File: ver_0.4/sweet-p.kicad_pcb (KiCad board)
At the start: 2 copper layers, 80 x 75 mm, 39 parts, among them J10 Micro_SD_Card, J2 Screw_Terminal_01x02, J3 Conn_01x04_Female, J4 Conn_01x04_Female, J5 Screw_Terminal_01x05, J7 Conn_01x06_Pin, U1 adafruit_tpl511x, U4 ssd1306, U7 ds3231, U8 P78A05-1000

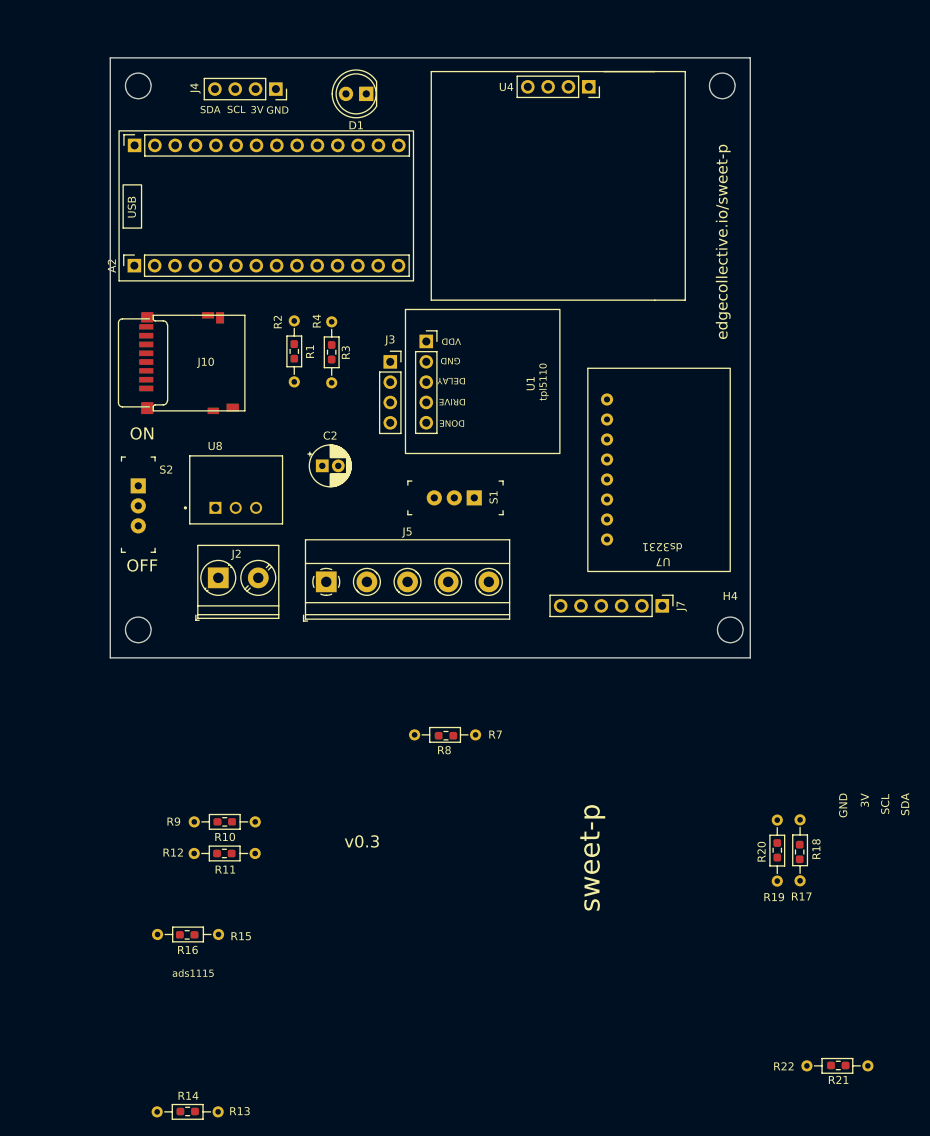
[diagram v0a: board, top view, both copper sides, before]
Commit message: pin assignments and initial layout for ver 0.4
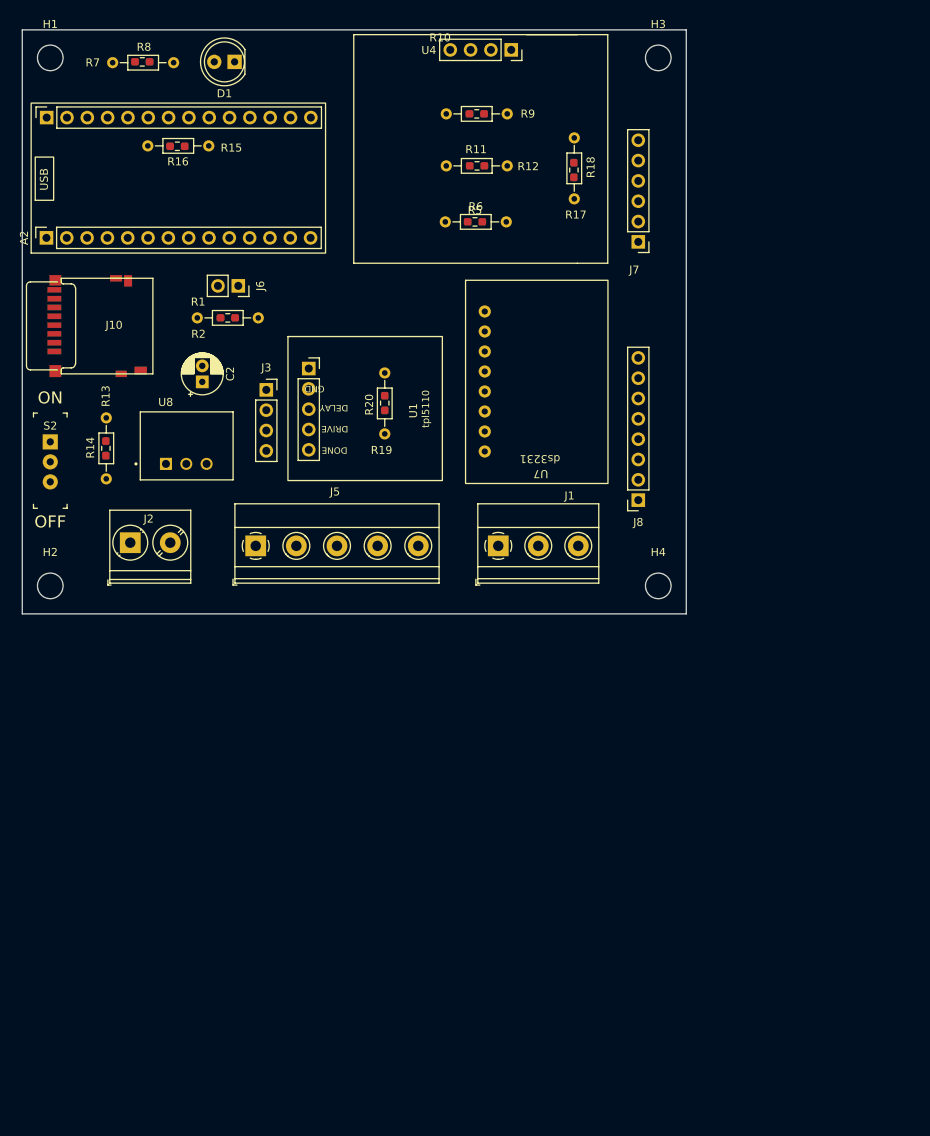
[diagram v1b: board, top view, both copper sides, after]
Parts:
- removed J4: Conn_01x04_Female, Connector_PinSocket_2.54mm:PinSocket_1x04_P2.54mm_Vertical
- removed R21: 10K, Resistor_SMD:R_0603_1608Metric_Pad0.98x0.95mm_HandSolder
- removed R22: R, Resistor_THT:R_Axial_DIN0204_L3.6mm_D1.6mm_P7.62mm_Horizontal
- removed R3: 4.7K, Resistor_SMD:R_0603_1608Metric_Pad0.98x0.95mm_HandSolder
- removed R4: 4.7K, Resistor_THT:R_Axial_DIN0204_L3.6mm_D1.6mm_P7.62mm_Horizontal
- removed S1: EG1218, digikey-footprints:Switch_Slide_11.6x4mm_EG1218
- added J1: Screw_Terminal_01x03, TerminalBlock_Phoenix:TerminalBlock_Phoenix_MKDS-1,5-3_1x03_P5.00mm_Horizontal, F.Cu at (85.0, 86.0)
- added J6: Conn_01x02_Socket, Connector_PinSocket_2.54mm:PinSocket_1x02_P2.54mm_Vertical, F.Cu at (52.5, 53.5)
- added J8: Conn_01x08_Socket, Connector_PinSocket_2.54mm:PinSocket_1x08_P2.54mm_Vertical, F.Cu at (102.5, 80.3)
- added R5: 4.7K, Resistor_SMD:R_0603_1608Metric_Pad0.98x0.95mm_HandSolder, F.Cu at (82.1, 45.5)
- added R6: 4.7K, Resistor_THT:R_Axial_DIN0204_L3.6mm_D1.6mm_P7.62mm_Horizontal, F.Cu at (78.4, 45.5)
- C2: value C_Polarized -> 330uF
- moved H2 104.7 mm to (29.0, 91.0)
- moved R16 98.6 mm to (44.9, 36.0)
- moved R15 98.6 mm to (41.2, 36.0)
- moved H3 96.6 mm to (105.0, 25.0)
- moved R7 95.5 mm to (36.8, 25.6), turned to 0 degrees
- moved R10 93.9 mm to (82.3, 32.0), turned to 0 degrees
- moved R8 92.4 mm to (40.5, 25.5), turned to 0 degrees
- moved R9 91.7 mm to (78.5, 32.0), turned to 0 degrees
- moved R11 91.6 mm to (82.3, 38.5), turned to 0 degrees
- moved R17 89.8 mm to (94.5, 42.6)
- moved R18 89.8 mm to (94.5, 39.0)
- moved R12 89.2 mm to (78.5, 38.5), turned to 0 degrees
- moved R14 83.5 mm to (36.0, 73.8), turned to 90 degrees
- moved R13 79.4 mm to (36.0, 77.6), turned to 90 degrees
- moved R19 74.4 mm to (70.8, 72.0)
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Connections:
- A2 pad 10: unconnected-(A2-A5-Pad10) -> A5
- A2 pad 11: unconnected-(A2-SCK-Pad11) -> SCK
- A2 pad 12: unconnected-(A2-M0-Pad12) -> MOSI
- A2 pad 13: unconnected-(A2-MI-Pad13) -> MISO
- A2 pad 14: unconnected-(A2-D2-Pad14) -> RX_D2
- A2 pad 20: unconnected-(A2-7-Pad20) -> DONE
- A2 pad 21: unconnected-(A2-9-Pad21) -> SAT_EN
- A2 pad 23: RX2 -> ONEWIRE_11
- A2 pad 24: TX2 -> D12
- A2 pad 4: unconnected-(A2-VHI-Pad4) -> VHI
- A2 pad 6: SAT_EN -> BATT_A1
- A2 pad 7: A1 -> A2
- A2 pad 8: DONE -> A3
- A2 pad 9: A4 -> TX_A4
- J10 pad 9: unconnected-(J10-SHIELD-Pad9) -> GND
- J5 pad 3: RX -> RX_D2
- J5 pad 4: TX -> TX_A4
- J5 pad 5: A4 -> D12
- J7 pad 4: TX2 -> TX
- J7 pad 5: RX2 -> RX
- R1 pad 1: Net-(R1-Pad1) -> Net-(J3-Pin_2)
- R13 pad 2: A1 -> BATT_A1
- R14 pad 2: A1 -> BATT_A1
- R15 pad 1: A1 -> BATT_A1
- R16 pad 1: A1 -> BATT_A1
- R2 pad 1: Net-(R1-Pad1) -> Net-(J3-Pin_2)
- U7 pad 7: RTC_INT -> unconnected-(U7-SQW-Pad7)
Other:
- board size 80 x 75 mm -> 83 x 73 mm
- board text removed: "3V"
- board text removed: "SCL"
- board text removed: "SDA"
- board text removed: "VDD"
- board text removed: "ads1115"
- board text removed: "edgecollective.io/sweet-p"
- board text removed: "sweet-p"
- board text removed: "v0.3"

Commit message: fully routed v4
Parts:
- moved J6 3.46 mm to (49.0, 53.5)
- moved R1 3.46 mm to (47.7, 57.5)
- moved R2 3.46 mm to (51.5, 57.5)
- moved R15 3.08 mm to (40.5, 39.0)
- moved R16 3.08 mm to (44.2, 39.0)
- moved U8 2.06 mm to (41.4, 75.5)
- moved C2 1.07 mm to (47.8, 64.5)
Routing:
- net GND: track 0.00 -> 320.9 mm, vias 0 -> 11
- net +3V3: track 0.00 -> 229.7 mm, vias 0 -> 13
- net SDA: track 0.00 -> 124.3 mm, vias 0 -> 8
- net 5V_TIMER: track 0.00 -> 112.9 mm, vias 0 -> 6
- net ONEWIRE_11: track 0.00 -> 107.1 mm, vias 0 -> 3
- net SCL: track 0.00 -> 105.0 mm, vias 0 -> 4
- net D12: track 0.00 -> 104.6 mm, vias 0 -> 2
- net 5V_DC: track 0.00 -> 90.7 mm, vias 0 -> 3
- net A0: track 0.00 -> 87.6 mm, vias 0 -> 1
- net A2: track 0.00 -> 87.4 mm, vias 0 -> 3
- net A3: track 0.00 -> 81.7 mm, vias 0 -> 3
- net SAT_EN: track 0.00 -> 71.3 mm, vias 0 -> 2
- net DONE: track 0.00 -> 68.4 mm, vias 0 -> 4
- net A5: track 0.00 -> 67.0 mm, vias 0 -> 2
- net TX_A4: track 0.00 -> 63.4 mm, vias 0 -> 2
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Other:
- board text added: "1W"
- board text added: "3V"
- board text added: "5V"
- board text added: "A0"
- board text added: "A2"
- board text added: "A3"
- board text added: "A5"
- board text added: "D12"
- board text added: "DRX"
- board text added: "DTX"
- board text added: "RX"
- board text added: "SCL"
- board text added: "SDA"
- board text added: "SEN"
- board text added: "TX"
- board text added: "VEXT"
- board text added: "itsybitsy"
- board text added: "p78a05-1000"
- board text added: "ssd1306"

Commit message: update
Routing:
- net D12: track 104.6 -> 99.6 mm, vias 2 -> 0
- net SCL: track 105.0 -> 107.2 mm
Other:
- board text added: "RX2"
- board text added: "TX2"
- board text added: "github.com/edgecollective/sweet-p"
- board text added: "sweet-p ver 0.4"
- board text removed: "DRX"
- board text removed: "DTX"
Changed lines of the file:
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@@
 	)
 	(gr_rect
+		(start 56 52.75)
+		(end 76.5 55.75)
+		(stroke
+			(width 0.15)
+			(type default)
+		)
+		(fill none)
+		(layer "F.SilkS")
+	)
+	(gr_rect
 		(start 25.5 21.5)
 		(end 108.5 94.5)
@@
 		(layer "Edge.Cuts")
 	)
+	(gr_text "github.com/edgecollective/sweet-p"
+		(at 105.6 79.9 -90)
+		(layer "B.SilkS")
+		(effects
+			(font
+				(size 1.5 1.5)
+				(thickness 0.3)
+				(bold yes)
+			)
+			(justify left bottom mirror)
+		)
+	)
 	(gr_text "1W"
 		(at 88.75 93.25 0)
@@
 		)
 	)
+	(gr_text "sweet-p ver 0.4"
+		(at 56.75 55 0)
+		(layer "F.SilkS")
+		(effects
+			(font
+				(size 1.5 1.5)
+				(thickness 0.3)
+				(bold yes)
+			)
+			(justify left bottom)
+		)
+	)
 	(gr_text "3V"
 		(at 104.75 48.5 0)
@@
 		)
 	)
-	(gr_text "DRX"
+	(gr_text "RX2"
 		(at 63.5 93.5 0)
 		(layer "F.SilkS")
@@
 		)
 	)
-	(gr_text "DTX"
+	(gr_text "TX2"
 		(at 68.5 93.5 0)
 		(layer "F.SilkS")
@@
 	)
 	(segment
-		(start 83.2575 38.5)
-		(end 86.12 38.5)
+		(start 89.002 71.162)
+		(end 90.5 72.66)
 		(width 0.4)
 		(layer "F.Cu")
@@
 	)
 	(segment
-		(start 55 36)
-		(end 83.62 36)
+		(start 83.2575 38.5)
+		(end 86.12 38.5)
 		(width 0.4)
 		(layer "F.Cu")
@@
 	)
 	(segment
-		(start 89.16 72.66)
-		(end 88.5 72)
+		(start 89 71.162)
+		(end 89.002 71.162)
 		(width 0.4)
 		(layer "F.Cu")
@@
 	)
 	(segment
-		(start 87 61.5)
-		(end 86.8 61.7)
+		(start 88.3 61.7)
+		(end 88.9 61.1)
 		(width 0.4)
 		(layer "F.Cu")
@@
 	)
 	(segment
-		(start 87.5 61.5)
-		(end 87 61.5)
+		(start 55 36)
+		(end 83.62 36)
 		(width 0.4)
 		(layer "F.Cu")
@@
 	)
 	(segment
-		(start 86.8 61.7)
-		(end 83.31 61.7)
+		(start 83.31 61.7)
+		(end 88.3 61.7)
 		(width 0.4)
 		(layer "F.Cu")
@@
 	(segment
 		(start 102.5 72.66)
-		(end 89.16 72.66)
+		(end 90.5 72.66)
 		(width 0.4)
 		(layer "F.Cu")
@@
 	)
 	(via
-		(at 87.5 61.5)
+		(at 89 71.162)
 		(size 0.8)
 		(drill 0.4)
@@
 	)
 	(via
-		(at 88.5 72)
+		(at 88.9 61.1)
 		(size 0.8)
 		(drill 0.4)
@@
 	)
 	(segment
-		(start 88.5 62.5)
-		(end 87.5 61.5)
+		(start 88.5 44.4)
+		(end 87.9 45)
+		(width 0.4)
+		(layer "B.Cu")
+		(net 9)
+	)
+	(segment
+		(start 87.9 46.1)
+		(end 88.9 47.1)
 		(width 0.4)
 		(layer "B.Cu")
@@
 	)
 	(segment
+		(start 88.9 69.562)
+		(end 88.9 71.062)
+		(width 0.4)
+		(layer "B.Cu")
+		(net 9)
+	)
+	(segment
 		(start 86.62 39)
 		(end 86.12 38.5)
@@
 	)
 	(segment
-		(start 87.5 61.5)
-		(end 87.5 39)
+		(start 88.9 61.1)
+		(end 88.9 70)
+		(width 0.4)
+		(layer "B.Cu")
+		(net 9)
+	)
+	(segment
+		(start 88.9 70)
+		(end 88.9 69.562)
+		(width 0.4)
+		(layer "B.Cu")
+		(net 9)
+	)
+	(segment
+		(start 88.5 40)
+		(end 88.5 40.4)
+		(width 0.4)
+		(layer "B.Cu")
+		(net 9)
+	)
+	(segment
+		(start 87.9 45)
+		(end 87.9 46.1)
+		(width 0.4)
+		(layer "B.Cu")
+		(net 9)
+	)
+	(segment
+		(start 87.5 39)
+		(end 88.5 40)
 		(width 0.4)
 		(layer "B.Cu")
@@
 	)
 	(segment
+		(start 88.9 71.062)
+		(end 89 71.162)
+		(width 0.4)
+		(layer "B.Cu")
+		(net 9)
+	)
+	(segment
 		(start 53.95 32.465)
 		(end 53.95 34.95)
@@
 	)
 	(segment
-		(start 88.5 72)
-		(end 88.5 62.5)
+		(start 88.9 47.1)
+		(end 88.9 61.1)
+		(width 0.4)
+		(layer "B.Cu")
+		(net 9)
+	)
+	(segment
+		(start 88.5 40.4)
+		(end 88.5 44.4)
 		(width 0.4)
 		(layer "B.Cu")
@@
 	)
 	(segment
-		(start 74 91)
-		(end 35.5 91)
-		(width 0.4)
-		(layer "F.Cu")
-		(net 26)
-	)
-	(segment
-		(start 35.5 91)
-		(end 34.5 90)
-		(width 0.4)
-		(layer "F.Cu")
-		(net 26)
-	)
-	(via
-		(at 74 91)
-		(size 0.8)
-		(drill 0.4)
-		(layers "F.Cu" "B.Cu")
-		(net 26)
-	)
-	(via
-		(at 34.5 90)
-		(size 0.8)
-		(drill 0.4)
-		(layers "F.Cu" "B.Cu")
-		(net 26)
-	)
-	(segment
-		(start 75 86)
-		(end 75 90)
+		(start 37.39 59.61)
+		(end 34.25 62.75)
 		(width 0.4)
 		(layer "B.Cu")
@@
 	)
 	(segment
-		(start 34.8 62.2)
-		(end 37.39 59.61)
+		(start 34.25 62.75)
+		(end 34.25 87.75)
 		(width 0.4)
 		(layer "B.Cu")
@@
 	)
 	(segment
-		(start 34.5 90)
-		(end 34.8 89.7)
+		(start 34.25 87.75)
+		(end 35.5 89)
 		(width 0.4)
 		(layer "B.Cu")
@@
 	)
 	(segment
-		(start 37.39 59.61)
-		(end 37.39 33.785)
+		(start 35.5 89)
+		(end 72 89)
 		(width 0.4)
 		(layer "B.Cu")
@@
 	)
 	(segment
-		(start 75 90)
-		(end 74 91)
+		(start 38.71 32.465)
+		(end 37.39 33.785)
 		(width 0.4)
 		(layer "B.Cu")
@@
 	(segment
 		(start 37.39 33.785)
-		(end 38.71 32.465)
+		(end 37.39 59.61)
 		(width 0.4)
 		(layer "B.Cu")
@@
 	)
 	(segment
-		(start 34.8 89.7)
-		(end 34.8 62.2)
+		(start 72 89)
+		(end 75 86)
 		(width 0.4)
 		(layer "B.Cu")
@@
 	)
 	(segment
-		(start 72.5 55)
-		(end 73.5 56)
-		(width 0.4)
-		(layer "F.Cu")
-		(net 29)
-	)
-	(segment
-		(start 62.5 55)
-		(end 72.5 55)
+		(start 72.75 56.75)
+		(end 73.5 57.5)
 		(width 0.4)
 		(layer "F.Cu")
@@
 		(net 29)
 	)
+	(segment
+		(start 62.75 56.75)
+		(end 72.75 56.75)
+		(width 0.4)
+		(layer "F.Cu")
+		(net 29)
+	)
 	(via
-		(at 73 80)
+		(at 62.75 56.75)
 		(size 0.8)
 		(drill 0.4)
@@
 	)
 	(via
-		(at 73.5 56)
+		(at 73 80)
 		(size 0.8)
 		(drill 0.4)
@@
 	)
 	(via
-		(at 62.5 55)
+		(at 73.5 57.5)
 		(size 0.8)
 		(drill 0.4)
@@
 	)
 	(segment
-		(start 73.5 56)
-		(end 73.5 79.5)
+		(start 61.54 52)
+		(end 61.54 54.04)
 		(width 0.4)
 		(layer "B.Cu")
@@
 	)
 	(segment
-		(start 61.54 52)
-		(end 61.54 54.04)
+		(start 64.84 82.16)
+		(end 64.84 86)
 		(width 0.4)
 		(layer "B.Cu")
@@
 	)
 	(segment
-		(start 64.84 82.16)
-		(end 64.84 86)
+		(start 61.54 54.04)
+		(end 61.54 55.54)
 		(width 0.4)
 		(layer "B.Cu")
@@
 	)
 	(segment
-		(start 61.54 54.04)
-		(end 62.5 55)
+		(start 61.54 55.54)
+		(end 62.75 56.75)
+		(width 0.4)
+		(layer "B.Cu")
+		(net 29)
+	)
+	(segment
+		(start 73.5 57.5)
+		(end 73.5 79.5)
 		(width 0.4)
 		(layer "B.Cu")
